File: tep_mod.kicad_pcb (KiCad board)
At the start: 2 copper layers, 53.5 x 48.5 mm, 3 parts, among them P2 CONN_01X04, U1 FONA_808

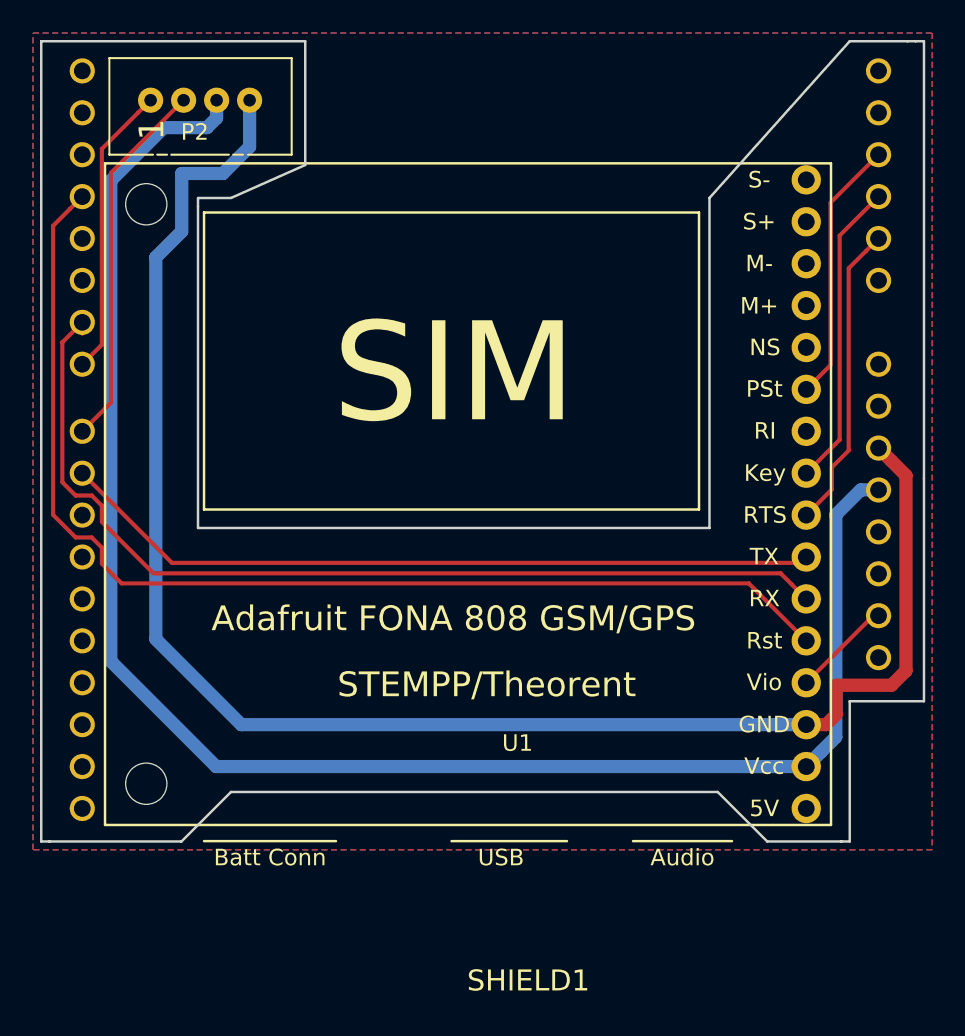
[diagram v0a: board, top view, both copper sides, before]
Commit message: Add logos in new graphics library
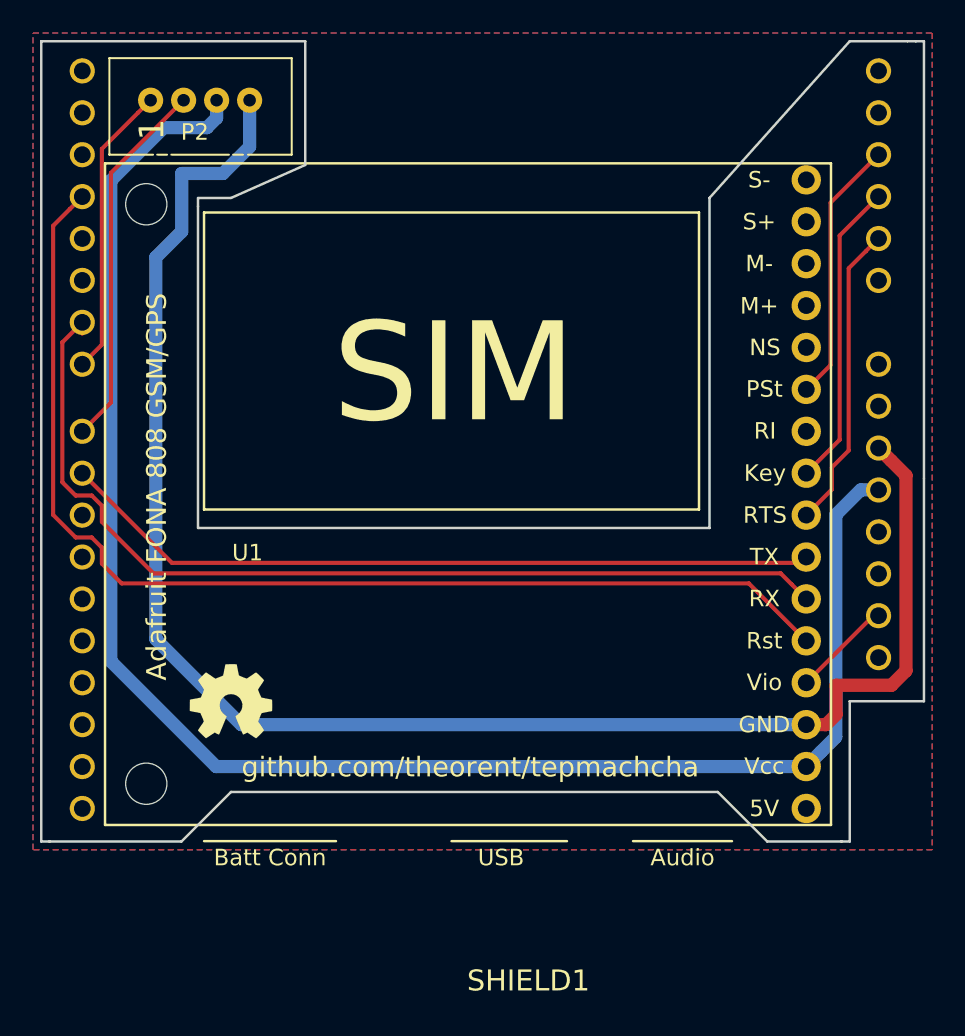
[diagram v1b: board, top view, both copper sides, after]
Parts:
- added G***: LOGO, Graphics:makerlab-logo, B.Cu at (133.7, 76.2)
- added G***: LOGO, Graphics:PIN-Logo, B.Cu at (106.7, 76.2)
- added G***: LOGO, Graphics:STEMPP-logo, B.Cu at (120.2, 76.2)
- added LOGO_OSHW_silkscreen_5mm: val**, freetronics_footprints:LOGO_OSHW_silkscreen_5mm, F.Cu at (106.7, 79.7)
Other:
- board text added: "github.com/theorent/tepmachcha"
- board text removed: "STEMPP/Theorent"

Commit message: Added Khmer script
Added Tepmachcha to board in Khmer OS script. Output directory change
(but it’s still local sorry)
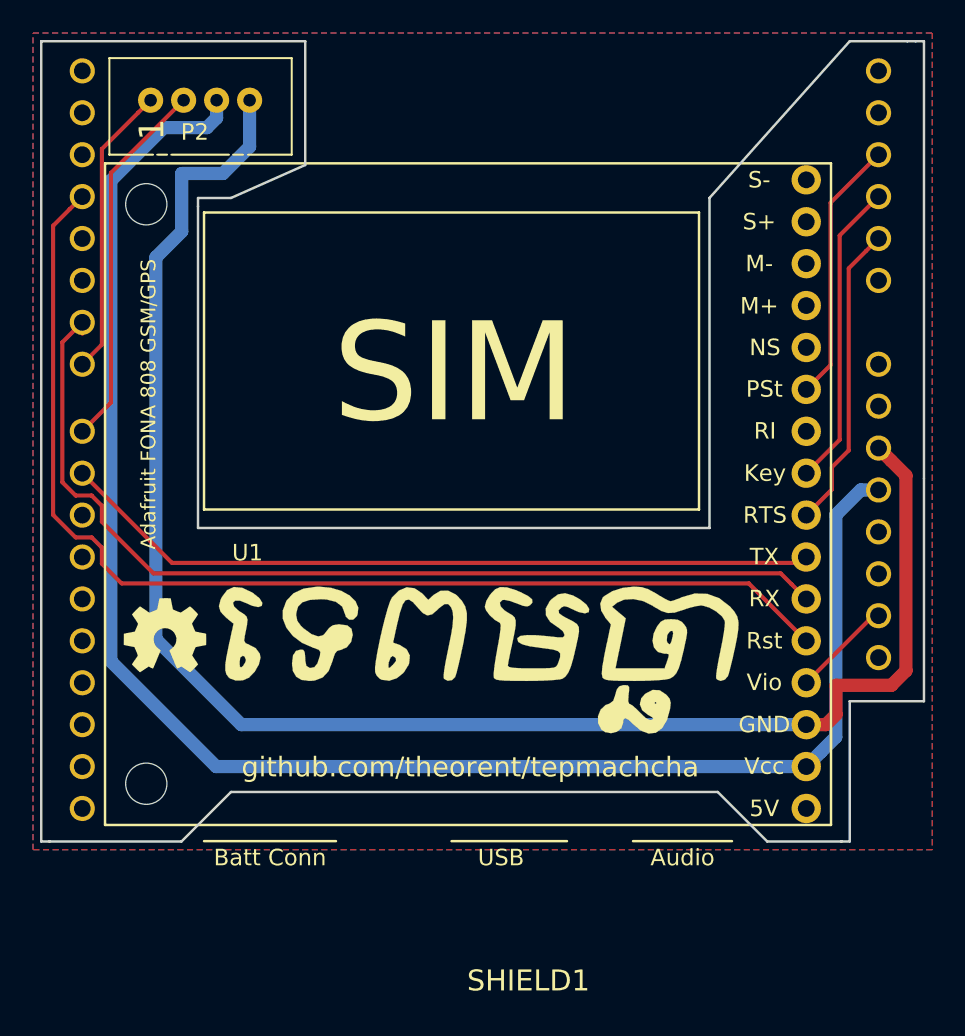
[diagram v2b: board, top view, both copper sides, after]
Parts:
- added G***: LOGO, Graphics:tepmachcha, F.Cu at (121.7, 77.2)
- moved LOGO_OSHW_silkscreen_5mm 5.66 mm to (102.7, 75.7)
